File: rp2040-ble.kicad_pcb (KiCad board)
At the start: 4 copper layers, 38 parts, among them J1 Conn_01x15, J2 Conn_01x15, J3 USB_B_Micro, J4 Conn_01x03, SW1 SW_Push, SW2 SW_Push, U1 RP2040, U2 W25Q128JVS, U3 HM-BT4502, U4 NCP1117DT33G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

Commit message: WIP Routing
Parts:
- removed R3: DNP, Resistor_SMD:R_0603_1608Metric
- added H1: MountingHole, MountingHole:MountingHole_2.2mm_M2, F.Cu at (164.2, 120.0)
- added H2: MountingHole, MountingHole:MountingHole_2.2mm_M2, F.Cu at (81.8, 71.4)
- added H3: MountingHole, MountingHole:MountingHole_2.2mm_M2, F.Cu at (162.6, 71.6)
- added H4: MountingHole, MountingHole:MountingHole_2.2mm_M2, F.Cu at (82.0, 120.2)
- C1, C10, C11, C12, C13, C14, C2, C3, C4, C5, C6, C7, C8, C9: footprint Capacitor_SMD:C_0603_1608Metric -> Capacitor_SMD:C_0402_1005Metric
- J1, J2: footprint Connector_PinSocket_1.27mm:PinSocket_1x15_P1.27mm_Vertical -> Connector_PinSocket_2.54mm:PinSocket_1x15_P2.54mm_Vertical
- J4: footprint Connector_PinSocket_1.27mm:PinSocket_1x03_P1.27mm_Vertical -> Connector_PinHeader_1.27mm:PinHeader_1x03_P1.27mm_Vertical
- R1, R2, R4, R5, R6, R7, R8: footprint Resistor_SMD:R_0603_1608Metric -> Resistor_SMD:R_0402_1005Metric
- Y1: value 12MHz -> ABLS-12.000MHZ-B4-T; footprint Crystal:Crystal_SMD_Abracon_ABM3-2Pin_5.0x3.2mm_HandSoldering -> ABLS-12:XTAL_ABLS-12.000MHZ-B4-T
- moved R2 75.3 mm to (143.4, 100.0), turned to 180 degrees
- moved J1 64.7 mm to (149.8, 72.8), turned to -90 degrees
- moved J2 62.4 mm to (147.4, 119.4), turned to -90 degrees
- moved R1 54.9 mm to (143.4, 98.8), turned to 180 degrees
- moved R8 52.9 mm to (141.9, 87.2), turned to 180 degrees
- moved U3 48.3 mm to (94.0, 75.6)
- moved C1 47.2 mm to (137.0, 93.2), turned to 0 degrees
- moved C12 46.5 mm to (139.2, 96.6), turned to 0 degrees
- moved C9 44.7 mm to (139.2, 97.8), turned to 0 degrees
- moved C8 44.1 mm to (140.2, 101.6), turned to -90 degrees
- moved C3 43.2 mm to (131.6, 91.4), turned to 90 degrees
- moved D1 42.2 mm to (133.2, 110.4), turned to 90 degrees
- moved C5 41.0 mm to (139.0, 101.6), turned to -90 degrees
- moved D2 39.6 mm to (143.4, 112.4)
- moved C2 38.2 mm to (137.8, 103.0), turned to -90 degrees
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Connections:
- J1 pad 1: /GPIO5 -> /VBUS
- J1 pad 10: /GPIO14 -> /GPIO8
- J1 pad 11: /GPIO15 -> /GPIO9
- J1 pad 12: /GPIO17 -> /GPIO10
- J1 pad 13: /GPIO18 -> GND
- J1 pad 14: /GPIO19 -> GND
- J1 pad 2: /GPIO6 -> /GPIO0
- J1 pad 3: /GPIO7 -> /GPIO1
- J1 pad 4: /GPIO8 -> /GPIO2
- J1 pad 5: /GPIO9 -> /GPIO3
- J1 pad 6: /GPIO10 -> /GPIO4
- J1 pad 7: /GPIO11 -> /GPIO5
- J1 pad 8: /GPIO12 -> /GPIO6
- J1 pad 9: /GPIO13 -> /GPIO7
- J2 pad 1: /VBUS -> /GPIO29
- J2 pad 10: /GPIO26 -> /GPIO20
- J2 pad 11: /GPIO27 -> /GPIO19
- J2 pad 12: /GPIO28 -> /GPIO18
- J2 pad 13: /GPIO29 -> /GPIO17
- J2 pad 14: GND -> /GPIO16
- J2 pad 3: GND -> /GPIO28
- J2 pad 4: GND -> /GPIO27
- J2 pad 5: /GPIO20 -> /GPIO26
- J2 pad 6: /GPIO21 -> /GPIO24
- J2 pad 7: /GPIO22 -> /GPIO23
- J2 pad 8: /GPIO23 -> /GPIO22
- J2 pad 9: /GPIO24 -> /GPIO21
- J4 pad 1: /SWCLK -> /SWD
- J4 pad 3: /SWD -> /SWCLK
- U1 pad 14: /GPIO11 -> /BLE_INT
- U1 pad 15: /GPIO12 -> /BLE_RX
- U1 pad 16: /GPIO13 -> /BLE_TX
- U1 pad 17: /GPIO14 -> /BLE_WAKEUP
- U1 pad 18: /GPIO15 -> /BLE_POWER_DOWN
- U1 pad 2: /BLE_RX -> /GPIO0
- U1 pad 3: /BLE_TX -> /GPIO1
- U1 pad 4: /BLE_WAKEUP -> /GPIO2
- U1 pad 5: /BLE_POWER_DOWN -> /GPIO3
- U1 pad 6: /BLE_INT -> /GPIO4
- Y1 pad 1: Net-(C13-Pad1) -> /XIN
- Y1 pad 2: /XIN -> Net-(C13-Pad1)
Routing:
- net /BLE_POWER_DOWN: track 0.00 -> 71.8 mm
- net /BLE_WAKEUP: track 0.00 -> 66.6 mm
- net /BLE_INT: track 0.00 -> 46.1 mm
- net /BLE_TX: track 0.00 -> 41.7 mm
- net /BLE_RX: track 0.00 -> 35.4 mm
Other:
- copper layers 4 -> 2

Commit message: PCB roouting
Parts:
- SW1, SW2: value SW_Push -> PTS810_SJK_250_SMTR_LFS; footprint Button_Switch_SMD:SW_SPST_B3S-1000 -> PTS810:PTS810 SJK 250 SMTR LFS
- moved U3 20.7 mm to (95.5, 96.2)
- moved H4 13.5 mm to (95.0, 124.0)
- moved H2 13.2 mm to (95.0, 72.0)
- moved C15 11.4 mm to (157.8, 104.0), turned to 90 degrees
- moved SW2 9.75 mm to (116.3, 115.0), turned to 0 degrees
- moved J4 9.52 mm to (106.6, 116.1), turned to 180 degrees
- moved C10 8.40 mm to (119.6, 95.0)
- moved C13 7.00 mm to (119.6, 101.0)
- moved R4 6.20 mm to (119.6, 103.6)
- moved H1 5.80 mm to (160.0, 124.0)
- moved J3 4.80 mm to (162.2, 99.2)
- moved D3 4.39 mm to (151.4, 101.8), turned to 0 degrees
- moved J2 3.99 mm to (150.0, 122.4)
- moved H3 2.63 mm to (160.0, 72.0)
- moved C3 2.41 mm to (131.8, 89.0), turned to 0 degrees
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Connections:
- J2 pad 1: /GPIO29 -> +3.3V
- J2 pad 2: +3.3V -> /GPIO29
- R6 pad 2: Net-(R6-Pad2) -> /USB_BOOT
- SW1 pad 1: GND -> /USB_BOOT
- SW1 pad 2: Net-(R6-Pad2) -> /USB_BOOT
- SW2 pad 1: GND -> /RUN
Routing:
- net +3.3V: track 0.00 -> 203.0 mm, vias 0 -> 8
- net GND: track 0.00 -> 49.9 mm, vias 0 -> 27
- net /VBUS: track 0.00 -> 38.4 mm, vias 0 -> 2
- net /SWD: track 0.00 -> 32.2 mm
- net /SWCLK: track 0.00 -> 30.2 mm
- net /GPIO0: track 0.00 -> 29.2 mm
- net /GPIO29: track 0.00 -> 27.9 mm
- net /GPIO1: track 0.00 -> 27.9 mm
- net /GPIO16: track 0.00 -> 27.4 mm
- net /GPIO2: track 0.00 -> 26.6 mm
- net /GPIO28: track 0.00 -> 25.8 mm
- net /GPIO17: track 0.00 -> 25.8 mm
- net /GPIO3: track 0.00 -> 25.7 mm
- net /GPIO10: track 0.00 -> 25.5 mm
- net /GPIO9: track 0.00 -> 24.6 mm
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- added copper zone on B.Cu, net GND
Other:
- board outline added: 75 x 62 mm

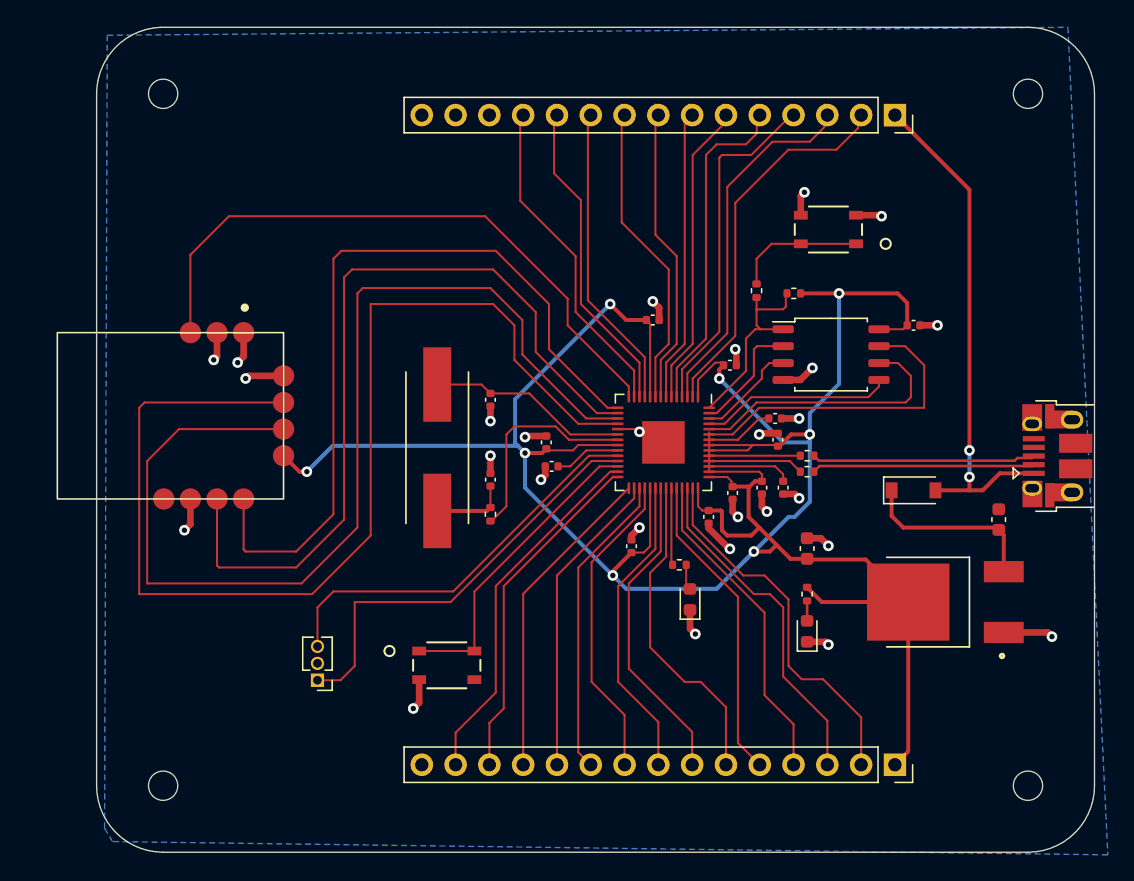
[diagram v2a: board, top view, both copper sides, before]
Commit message: Updated routing, addedd 3d models for parts
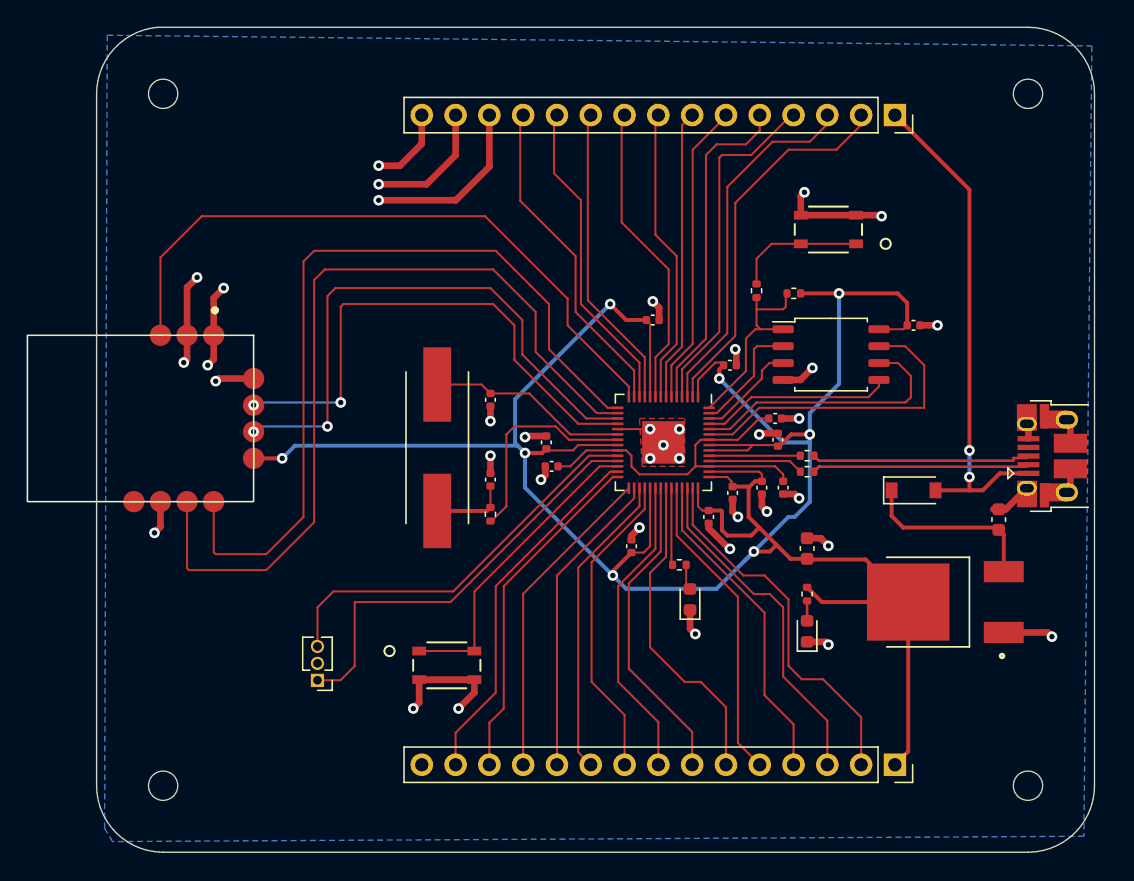
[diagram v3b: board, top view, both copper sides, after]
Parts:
- moved U3 2.26 mm to (93.3, 96.4)
- moved J3 0.40 mm to (161.8, 99.2)
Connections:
- J3 pad 2: /USB_D- -> /USB_CONN_D-
- J3 pad 3: /USB_D+ -> /USB_CONN_D+
- R1 pad 1: /USB_D+ -> /USB_CONN_D+
- R1 pad 2: Net-(R1-Pad2) -> /USB_D+
- R2 pad 1: /USB_D- -> /USB_CONN_D-
- R2 pad 2: Net-(R2-Pad2) -> /USB_D-
- U1 pad 46: Net-(R2-Pad2) -> /USB_D-
- U1 pad 47: Net-(R1-Pad2) -> /USB_D+
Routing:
- net GND: track 49.9 -> 109.3 mm, vias 27 -> 37
- net /BLE_POWER_DOWN: track 85.5 -> 40.0 mm, vias 0 -> 2
- net /BLE_WAKEUP: track 80.9 -> 43.2 mm, vias 0 -> 2
- net /USB_CONN_D-: track 0.00 -> 17.1 mm
- net /USB_CONN_D+: track 0.00 -> 16.5 mm
- net +1V1: track 16.3 -> 27.4 mm
- net /USB_D+: track 16.8 -> 6.85 mm
- net /USB_D-: track 16.7 -> 7.38 mm
- net Net-(R2-Pad2): track 7.38 -> 0.00 mm
- net Net-(R1-Pad2): track 6.85 -> 0.00 mm
- net /BLE_TX: track 61.5 -> 63.8 mm
- net /BLE_INT: track 47.2 -> 49.6 mm
- net /BLE_RX: track 59.5 -> 61.8 mm
- net +3.3V: track 203.0 -> 201.3 mm
- net /GPIO5: track 22.7 -> 22.0 mm
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- added copper zone on F.Cu, net GND
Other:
- outline, holes or cut-outs redrawn

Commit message: Add gerbers, fix pcb issues
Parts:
- R1, R2, R4, R5, R6, R7, R8: footprint Resistor_SMD:R_0402_1005Metric -> Resistor_SMD:R_0603_1608Metric
- moved D1 2.15 mm to (135.4, 112.0)
- moved R5 1.71 mm to (134.4, 109.0)
- moved D2 0.60 mm to (143.4, 113.0)
- moved R2 0.46 mm to (143.6, 100.8)
- moved C8 0.40 mm to (141.2, 101.6)
- moved D3 0.40 mm to (151.4, 102.2)
- moved R1 0.28 mm to (143.6, 99.0)
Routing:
- net /GPIO25: track 5.80 -> 7.52 mm
- net /USB_CONN_D-: track 17.1 -> 16.1 mm
- net Net-(D1-Pad2): track 1.93 -> 2.70 mm
- net Net-(D2-Pad2): track 1.50 -> 2.10 mm
- removed copper zone on F.Cu, net GND
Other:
- board text added: "+"
- board text added: "+3.3v"
- board text added: "BLE INT / GPIO11"
- board text added: "BLE POWER / GPIO15 Down"
- board text added: "BLE RX / GPIO12"
- board text added: "BLE TX / GPIO13"
- board text added: "BLE Wakeup / GPIO14"
- board text added: "BOOTSEL"
- board text added: "FLASH"
- board text added: "GND"
- board text added: "GPIO0"
- board text added: "GPIO1"
- board text added: "GPIO10"
- board text added: "GPIO16"
- board text added: "GPIO17"
- board text added: "GPIO18"
- board text added: "GPIO19"
- board text added: "GPIO2"
- board text added: "GPIO20"
- board text added: "GPIO21"
- board text added: "GPIO22"
- board text added: "GPIO23"
- board text added: "GPIO24"
- board text added: "GPIO25"
- board text added: "GPIO26"
- board text added: "GPIO27"
- board text added: "GPIO28"
- board text added: "GPIO29"
- board text added: "GPIO3"
- board text added: "GPIO4"
- board text added: "GPIO5"
- board text added: "GPIO6"
- board text added: "GPIO7"
- board text added: "GPIO8"
- board text added: "GPIO9"
- board text added: "Power LED"
- board text added: "RP2040 BLE Rev1"
- board text added: "Reset"
- board text added: "SWCLK"
- board text added: "SWD"
- board text added: "USB"
- board text added: "USER LED"
- board text added: "VBUS"
